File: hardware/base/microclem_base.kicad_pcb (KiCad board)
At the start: 2 copper layers, 160 x 100 mm, 85 parts, among them U1 74AHC02, U10 74AHC74, U11 74AHC74, U12 74AHC14, U13 74AHC08, U14 74AC32, U15 74HC590, U16 74AC163, U17 74AC163, U18 74AHCT245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

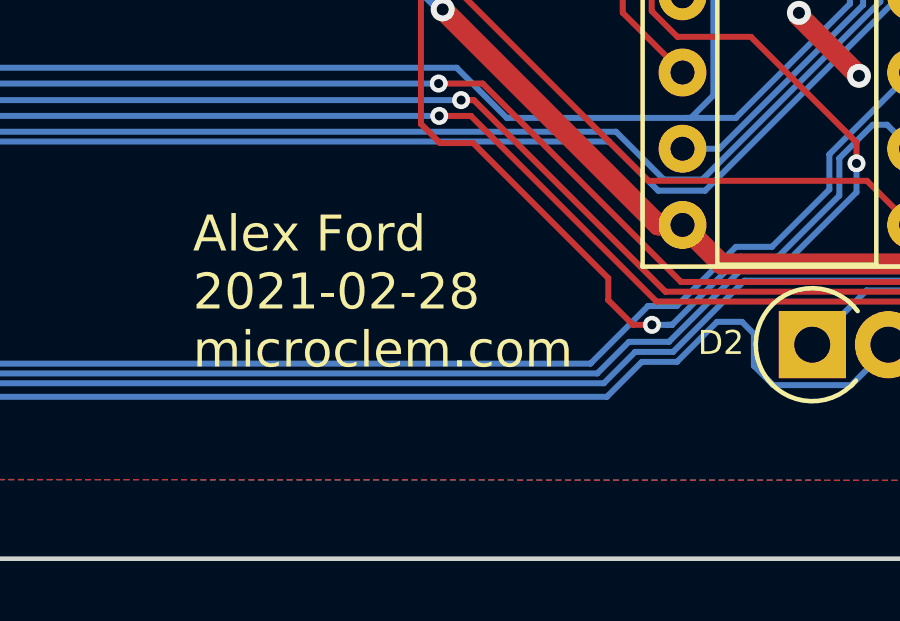
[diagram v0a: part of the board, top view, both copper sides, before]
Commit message: remove an unused library
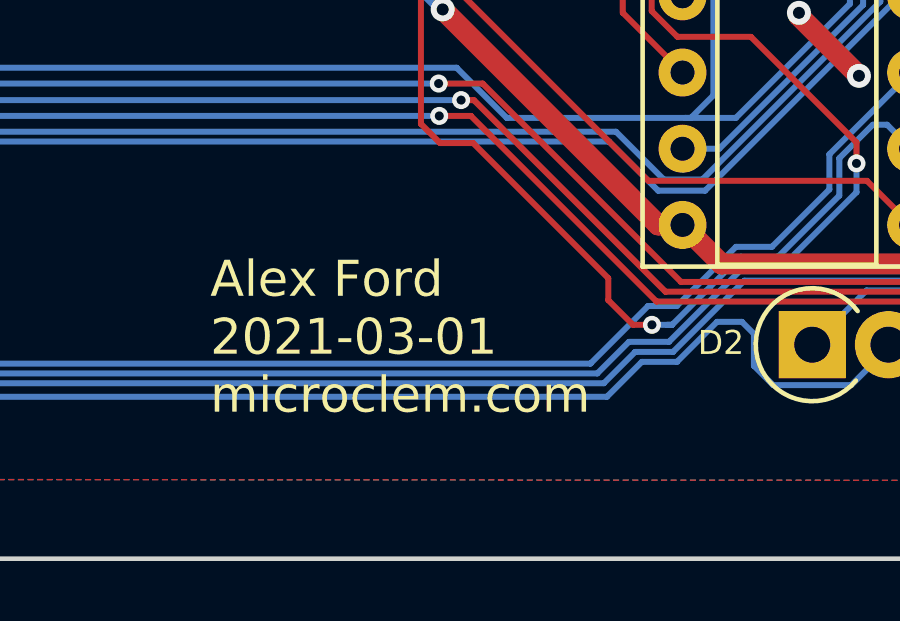
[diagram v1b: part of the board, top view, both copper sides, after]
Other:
- board text added: "Alex Ford 2021-03-01 microclem.com"
- board text removed: "Alex Ford 2021-02-28 microclem.com"

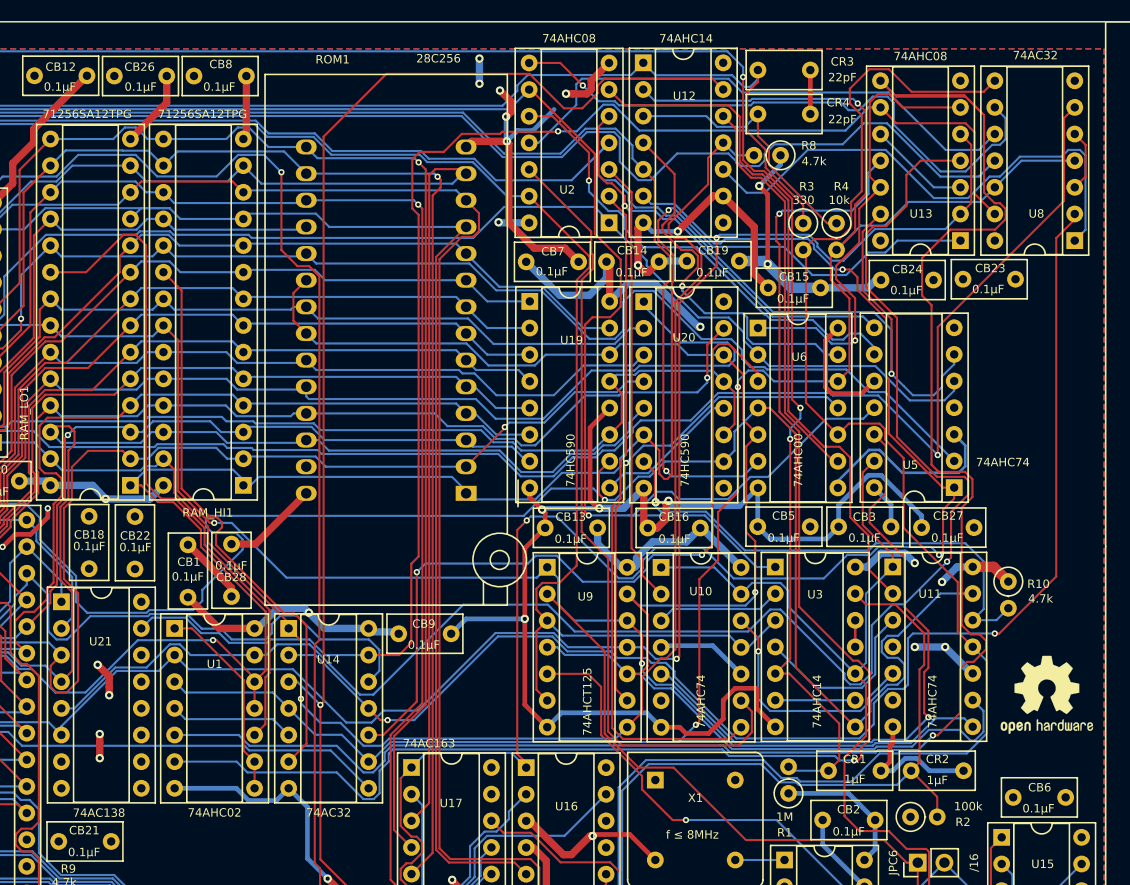
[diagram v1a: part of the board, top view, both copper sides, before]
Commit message: base: update specific 74 part references
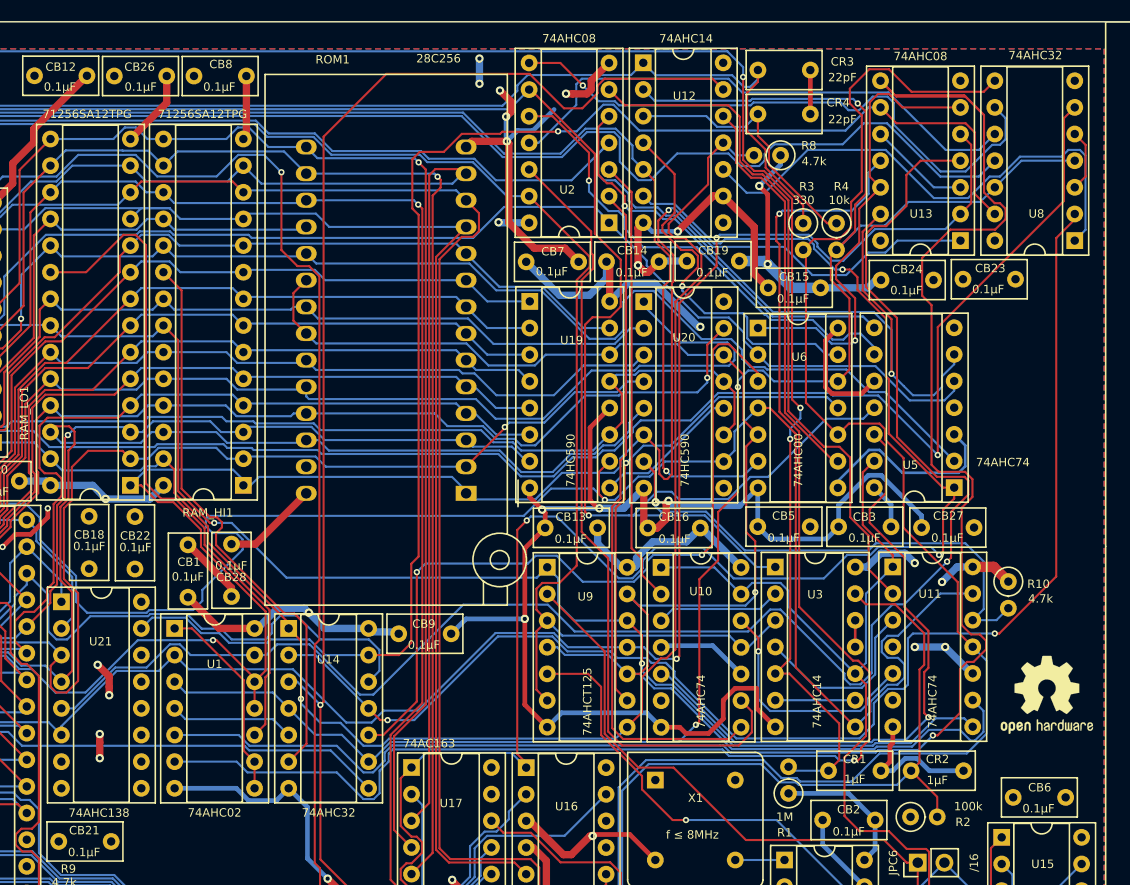
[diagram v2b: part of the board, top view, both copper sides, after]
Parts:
- U14, U8: value 74AC32 -> 74AHC32
- U21: value 74AC138 -> 74AHC138

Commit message: base: relayout WIP
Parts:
- removed CB2, CB27, CB3, CB4, CB5, CB7: 0.1μF, Capacitor_THT:C_Rect_L7.0mm_W3.5mm_P5.00mm
- removed CR1, CR2: 1μF, Capacitor_THT:C_Rect_L7.0mm_W3.5mm_P5.00mm
- removed D1, D2: DIODE, Diode_THT:D_DO-15_P2.54mm_Vertical_AnodeUp
- removed DR1: eurocard_end_mount, din61412:eurocard_end_mount
- removed JPC1: JP_RST, Connector_PinHeader_2.54mm:PinHeader_1x02_P2.54mm_Vertical
- removed JPC2: /1, Connector_PinHeader_2.54mm:PinHeader_1x02_P2.54mm_Vertical
- removed JPC3: /2, Connector_PinHeader_2.54mm:PinHeader_1x02_P2.54mm_Vertical
- removed JPC4: /4, Connector_PinHeader_2.54mm:PinHeader_1x02_P2.54mm_Vertical
- removed JPC5: /8, Connector_PinHeader_2.54mm:PinHeader_1x02_P2.54mm_Vertical
- removed JPC6: /16, Connector_PinHeader_2.54mm:PinHeader_1x02_P2.54mm_Vertical
- removed R1: 1M, Resistor_THT:R_Axial_DIN0207_L6.3mm_D2.5mm_P2.54mm_Vertical
- removed R2: 100k, Resistor_THT:R_Axial_DIN0207_L6.3mm_D2.5mm_P2.54mm_Vertical
- removed R6: 4.7k, Resistor_THT:R_Axial_DIN0207_L6.3mm_D2.5mm_P2.54mm_Vertical
- removed U10, U11: 74AHC74, Package_DIP:DIP-14_W7.62mm_Socket
- removed U2, U4: 74AHC08, Package_DIP:DIP-14_W7.62mm_Socket
- removed U3: 74AHC14, Package_DIP:DIP-14_W7.62mm_Socket
- removed X1: CXO_DIP8, Oscillator:Oscillator_DIP-8
- LOGO1: renamed from G***; value LOGO -> Logo_Microclem
- LOGO2: renamed from G***; value LOGO -> Logo_QR_Code
- LOGO3: renamed from REF**; value OSHW-Logo2_9.8x8mm_SilkScreen -> Logo_Open_Hardware_Small
- moved LOGO1 89.8 mm to (169.5, 133.0)
- moved LOGO3 49.8 mm to (202.8, 120.9)
- moved U15 33.5 mm to (129.5, 95.1)
- moved CB6 31.8 mm to (137.4, 90.9)
- moved LOGO2 27.8 mm to (122.5, 140.5)
- moved R10 17.2 mm to (161.9, 58.4)
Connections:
- CONN1 pad A28: SYS_CLK -> PHI_2
- CONN1 pad B28: SYS_CLK -> PHI_2
- CONN1 pad C31: ~RST_HDR~ -> BASE_CLK
- MP1 pad 37: PHI_2 -> BOARD_CLK
- R3 pad 2: PHI_2 -> BOARD_CLK
- U15 pad 10: ~CLK_RST~ -> ~RST~
- U15 pad 11: Net-(JPC2-Pad2) -> PHI_2
- U15 pad 13: Net-(JPC2-Pad2) -> PHI_2
- U5 pad 11: BUS_CLK -> BOARD_CLK
- U5 pad 12: Net-(U10-Pad5) -> Net-(R10-Pad2)
- U5 pad 13: ~CLK_RST~ -> ~RST~
- U5 pad 8: Net-(U2-Pad5) -> CPY
- U5 pad 9: Net-(U2-Pad10) -> ~CPY~
- U6 pad 10: PHI_2 -> BOARD_CLK
- U7 pad 12: PHI_2 -> BOARD_CLK
- U7 pad 9: PHI_2 -> BOARD_CLK
- U8 pad 10: Net-(U2-Pad11) -> GND
- U8 pad 8: PHI_2 -> Net-(U8-Pad8)
- U8 pad 9: Net-(U2-Pad8) -> GND
- U9 pad 2: Net-(JPC2-Pad1) -> PHI_2
- U9 pad 3: SYS_CLK -> BOARD_CLK
- U9 pad 6: SYS_CLK -> BOARD_CLK
- VIA1 pad 25: PHI_2 -> BOARD_CLK
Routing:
- net PHI_2: track 330.2 -> 2.54 mm, vias 1 -> 0
- net ~RST_HDR~: track 195.9 -> 0.00 mm, vias 1 -> 0
- net BUS_CLK: track 190.5 -> 2.54 mm, vias 1 -> 0
- net SYS_CLK: track 179.8 -> 0.00 mm
- net Net-(CR1-Pad1): track 178.4 -> 0.00 mm, vias 3 -> 0
- net /S_ROM: track 172.8 -> 0.00 mm, vias 1 -> 0
- net ~BUS_ACTIVE~: track 215.4 -> 61.7 mm
- net ~CLK_RST~: track 134.1 -> 0.00 mm
- net Net-(CR3-Pad1): track 135.7 -> 17.2 mm, vias 1 -> 0
- net GND: track 431.6 -> 313.4 mm, vias 28 -> 24
- net BOARD_CLK: track 0.00 -> 112.7 mm, vias 0 -> 1
- net Net-(CR2-Pad1): track 90.5 -> 0.00 mm
- net +5V: track 219.1 -> 138.1 mm, vias 15 -> 8
- net Net-(U10-Pad9): track 75.8 -> 0.00 mm
- net Net-(U11-Pad2): track 66.4 -> 0.00 mm
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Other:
- board text removed: "f ≤ 8MHz"
